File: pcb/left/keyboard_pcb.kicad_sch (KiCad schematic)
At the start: 42 parts, among them K00 KEYSW, K01 KEYSW, K02 KEYSW, K03 KEYSW, K04 KEYSW, K05 KEYSW, K10 KEYSW, K11 KEYSW, K12 KEYSW, K13 KEYSW, K14 KEYSW, K15 KEYSW, K20 KEYSW, K21 KEYSW, K22 KEYSW, K23 KEYSW, K24 KEYSW, K25 KEYSW, K30 KEYSW, K31 KEYSW, K32 KEYSW, U1 Flippable RP2040 ProMicro/nic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

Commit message: Update matrix schematic
 * Add diodes
 * Add 5-way nav. switches
 * Duplicate left to right
 * Tidy layout
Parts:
- added 右D00, 右D01, 右D02, 右D03, 右D04, 右D05, 右D10, 右D11, 右D12, 右D13, 右D14, 右D15, 右D20, 右D21, 右D22, 右D23, 右D24, 右D25, 右D32, 右D33, 右D34, 右D35, 右D40, 右D41, 右D42, 右D43, 右D44, 左D00, 左D01, 左D02, 左D03, 左D04, 左D05, 左D10, 左D11, 左D12, 左D13, 左D14, 左D15, 左D20, 左D21, 左D22, 左D23, 左D24, 左D25, 左D32, 左D33, 左D34, 左D35, 左D40, 左D41, 左D42, 左D43, 左D44: D, symbol Device:D
- added 右K00, 右K01, 右K02, 右K03, 右K04, 右K05, 右K10, 右K11, 右K12, 右K13, 右K14, 右K15, 右K20, 右K21, 右K22, 右K23, 右K24, 右K25, 右K33, 右K34, 右K35: KEYSW, keyswitches:SW_PG1350_reversible, symbol Switch:SW_Push
- added 右K43, 右K45, 左K43, 左K45: SW_SP5T, symbol _Project Library:SW_SP5T
- 左K00: renamed from K00; symbol keyboard_parts:KEYSW -> Switch:SW_Push
- 左K01: renamed from K01; symbol keyboard_parts:KEYSW -> Switch:SW_Push
- 左K02: renamed from K02; symbol keyboard_parts:KEYSW -> Switch:SW_Push
- 左K03: renamed from K03; symbol keyboard_parts:KEYSW -> Switch:SW_Push
- 左K04: renamed from K04; symbol keyboard_parts:KEYSW -> Switch:SW_Push
- 左K05: renamed from K05; symbol keyboard_parts:KEYSW -> Switch:SW_Push
- 左K10: renamed from K10; symbol keyboard_parts:KEYSW -> Switch:SW_Push
- 左K11: renamed from K11; symbol keyboard_parts:KEYSW -> Switch:SW_Push
- 左K12: renamed from K12; symbol keyboard_parts:KEYSW -> Switch:SW_Push
- 左K13: renamed from K13; symbol keyboard_parts:KEYSW -> Switch:SW_Push
- 左K14: renamed from K14; symbol keyboard_parts:KEYSW -> Switch:SW_Push
- 左K15: renamed from K15; symbol keyboard_parts:KEYSW -> Switch:SW_Push
- 左K20: renamed from K20; symbol keyboard_parts:KEYSW -> Switch:SW_Push
- 左K21: renamed from K21; symbol keyboard_parts:KEYSW -> Switch:SW_Push
- 左K22: renamed from K22; symbol keyboard_parts:KEYSW -> Switch:SW_Push
- 左K23: renamed from K23; symbol keyboard_parts:KEYSW -> Switch:SW_Push
- 左K24: renamed from K24; symbol keyboard_parts:KEYSW -> Switch:SW_Push
- 左K25: renamed from K25; symbol keyboard_parts:KEYSW -> Switch:SW_Push
- 左K33: renamed from K30; symbol keyboard_parts:KEYSW -> Switch:SW_Push
- 左K34: renamed from K31; symbol keyboard_parts:KEYSW -> Switch:SW_Push
- 左K35: renamed from K32; symbol keyboard_parts:KEYSW -> Switch:SW_Push
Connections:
- net col6 is gone; now on net col5: U1.24 (GP21/GP9)
- net k01 is gone; now on net col1: 左K01.1
- net k02 is gone; now on net col2: 左K02.1
- net k03 is gone; now on net col3: 左K03.1
- net k04 is gone; now on net col4: 左K04.1
- net k05 is gone; now on net col5: 左K05.1
- net k10 is gone; now on net col0: 左K10.1
- net k11 is gone; now on net col1: 左K11.1
- net k12 is gone; now on net col2: 左K12.1
- net k13 is gone; now on net col3: 左K13.1
- net k14 is gone; now on net col4: 左K14.1
- net k15 is gone; now on net col5: 左K15.1
- net k20 is gone; now on net col0: 左K20.1
- net k21 is gone; now on net col1: 左K21.1
- net k22 is gone; now on net col2: 左K22.1
- net k23 is gone; now on net col3: 左K23.1
- net k24 is gone; now on net col4: 左K24.1
- net k25 is gone; now on net col5: 左K25.1
- net k30 is gone; now on net col3: 左K33.1
- net k31 is gone; now on net col4: 左K34.1
- net k32 is gone; now on net col5: 左K35.1
- net row5 is gone; now on net row4: U1.12 (GP9/GP21)
- net GND: no longer 左K00.2, 左K01.2, 左K02.2, 左K03.2, 左K04.2, 左K05.2, 左K10.2, 左K11.2, 左K12.2, 左K13.2, 左K14.2, 左K15.2, 左K20.2, 左K21.2, 左K22.2, 左K23.2, 左K24.2, 左K25.2, 左K33.2, 左K34.2, 左K35.2
- net col1: now also U1.20 (GP26/GP5), 右D41.2 (A), 右K01.1, 右K11.1, 右K21.1, 左D41.2 (A); no longer U1.19 (GP27/GP4)
- net col2: now also U1.21 (GP22/GP6), 右E1.S1, 左E1.S1, 右D42.2 (A), 右K02.1, 右K12.1, 右K22.1, 左D42.2 (A); no longer U1.20 (GP26/GP5)
- net col3: now also U1.22 (GP20/GP7), 右D43.2 (A), 右K03.1, 右K13.1, 右K23.1, 右K33.1, 左D43.2 (A); no longer U1.21 (GP22/GP6)
- net col4: now also U1.23 (GP23/GP8), 右D44.2 (A), 右K04.1, 右K14.1, 右K24.1, 右K34.1, 左D44.2 (A); no longer U1.22 (GP20/GP7)
- net col5: now also 右K05.1, 右K15.1, 右K25.1, 右K35.1; no longer U1.23 (GP23/GP8)
- net row1: now also U1.9 (GP6/GP22), 右D10.1 (K), 右D11.1 (K), 右D12.1 (K), 右D13.1 (K), 右D14.1 (K), 右D15.1 (K), 左D10.1 (K), 左D11.1 (K), 左D12.1 (K), 左D13.1 (K), 左D14.1 (K), 左D15.1 (K); no longer U1.8 (GP5/GP26)
- net row2: now also U1.10 (GP7/GP20), 右D20.1 (K), 右D21.1 (K), 右D22.1 (K), 右D23.1 (K), 右D24.1 (K), 右D25.1 (K), 左D20.1 (K), 左D21.1 (K), 左D22.1 (K), 左D23.1 (K), 左D24.1 (K), 左D25.1 (K); no longer U1.9 (GP6/GP22)
- net row3: now also U1.11 (GP8/GP23), 右D32.1 (K), 右D33.1 (K), 右D34.1 (K), 右D35.1 (K), 左D32.1 (K), 左D33.1 (K), 左D34.1 (K), 左D35.1 (K); no longer U1.10 (GP7/GP20)
- net row4: now also 右K43.1, 右K45.1, 左K43.1, 左K45.1; no longer U1.11 (GP8/GP23)
- net at 右E1.S2: now also 右D32.2 (A)
- net at 左E1.S2: now also 左D32.2 (A)
- net k00 renamed col0
- net col0: now also U1.19 (GP27/GP4), 右D40.2 (A), 右K00.1, 右K10.1, 右K20.1, 左D40.2 (A)
- new net: 右D21.2 (A), 右K21.2
- new net: 左D35.2 (A), 左K35.2
- new net: 左D13.2 (A), 左K13.2
- new net: 右D22.2 (A), 右K22.2
- new net: 左D24.2 (A), 左K24.2
- new net: 右D00.2 (A), 右K00.2
- new net: 右D23.2 (A), 右K23.2
- new net: 左D05.2 (A), 左K05.2
- new net: 右D25.2 (A), 右K25.2
- new net: 右D01.2 (A), 右K01.2
- new net: 右D02.2 (A), 右K02.2
- new net: 左D20.2 (A), 左K20.2
- new net: 左D11.2 (A), 左K11.2
- new net: 右D34.2 (A), 右K34.2
- new net: 右D24.2 (A), 右K24.2
- new net: 右D35.2 (A), 右K35.2
- new net: 左D00.2 (A), 左K00.2
- new net: 右D20.2 (A), 右K20.2
- new net: 右D14.2 (A), 右K14.2
- new net: 左D14.2 (A), 左K14.2
- new net: 左D15.2 (A), 左K15.2
- new net: 左D42.1 (K), 左K43.4, 左K45.4
- new net: 右D03.2 (A), 右K03.2
- new net: 右D33.2 (A), 右K33.2
- new net: 右D04.2 (A), 右K04.2
- new net: 右D41.1 (K), 右K43.3, 右K45.3
- new net: 右D05.2 (A), 右K05.2
- new net: 左D03.2 (A), 左K03.2
- new net: 右D44.1 (K), 右K43.6, 右K45.6
- new net: 左D43.1 (K), 左K43.5, 左K45.5
- new net: 左D22.2 (A), 左K22.2
- new net: 左D40.1 (K), 左K43.2, 左K45.2
- new net: 左D41.1 (K), 左K43.3, 左K45.3
- new net: 左D44.1 (K), 左K43.6, 左K45.6
- new net: 左D02.2 (A), 左K02.2
- new net: 右D13.2 (A), 右K13.2
- new net: 左D33.2 (A), 左K33.2
- new net: 右D43.1 (K), 右K43.5, 右K45.5
- new net: 右D42.1 (K), 右K43.4, 右K45.4
- new net: 右D11.2 (A), 右K11.2
- new net: 左D04.2 (A), 左K04.2
- new net: 左D12.2 (A), 左K12.2
- new net: 左D23.2 (A), 左K23.2
- new net: 右D10.2 (A), 右K10.2
- new net: 左D25.2 (A), 左K25.2
- new net: 右D12.2 (A), 右K12.2
- new net: 左D10.2 (A), 左K10.2
- new net: 左D01.2 (A), 左K01.2
- new net: 左D34.2 (A), 左K34.2
- new net: 右D40.1 (K), 右K43.2, 右K45.2
- new net: 左D21.2 (A), 左K21.2
- new net: 右D15.2 (A), 右K15.2
- new net row0: U1.8 (GP5/GP26), 右D00.1 (K), 右D01.1 (K), 右D02.1 (K), 右D03.1 (K), 右D04.1 (K), 右D05.1 (K), 左D00.1 (K), 左D01.1 (K), 左D02.1 (K), 左D03.1 (K), 左D04.1 (K), 左D05.1 (K)
- no-connect marks 0 -> 2
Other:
- moved on the sheet: H1, H2, H3, H4, MB1, MB2, MB3, MB4, U1, 右J1, 右J2, 右L2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

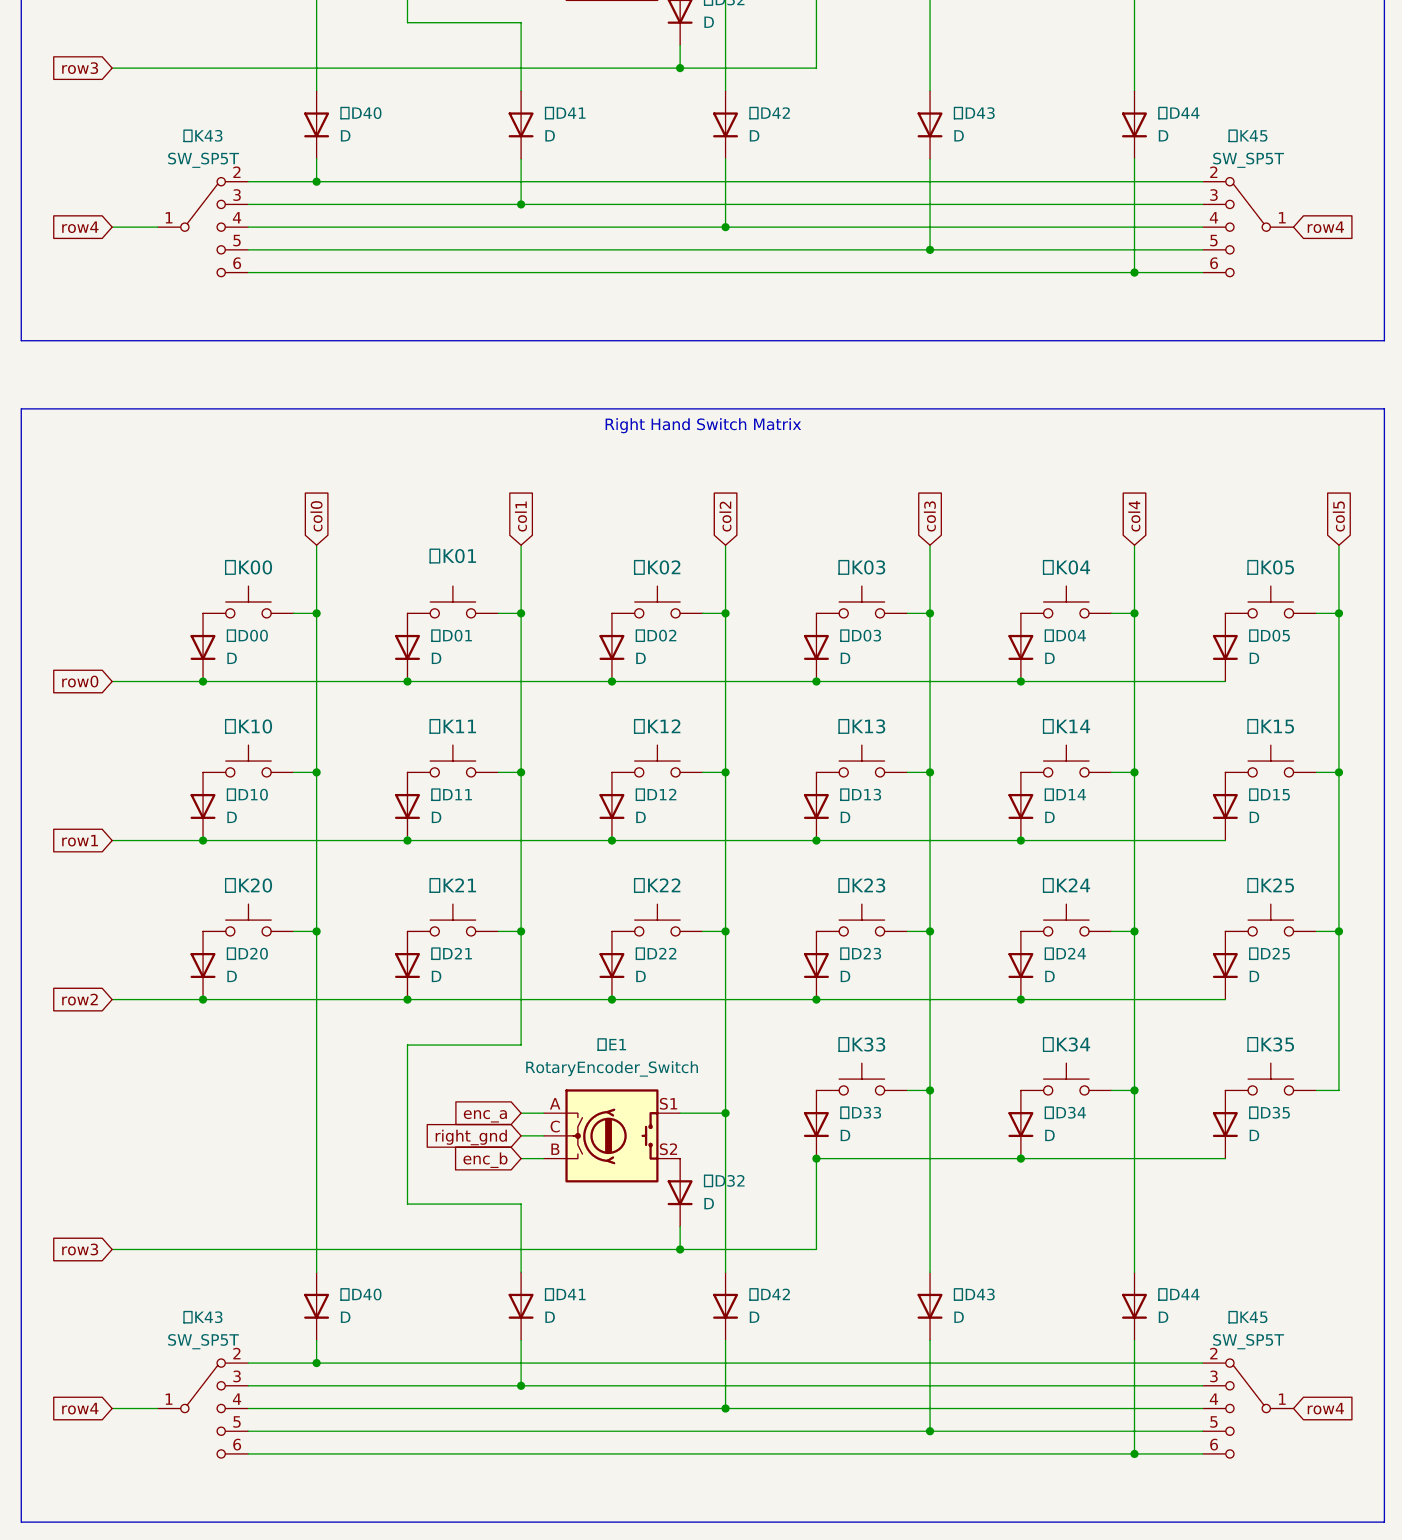
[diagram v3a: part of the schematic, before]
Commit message: Update nav. switch symbol to match datasheet
https://www.mouser.com/datasheet/2/15/SKRH-1370966.pdf
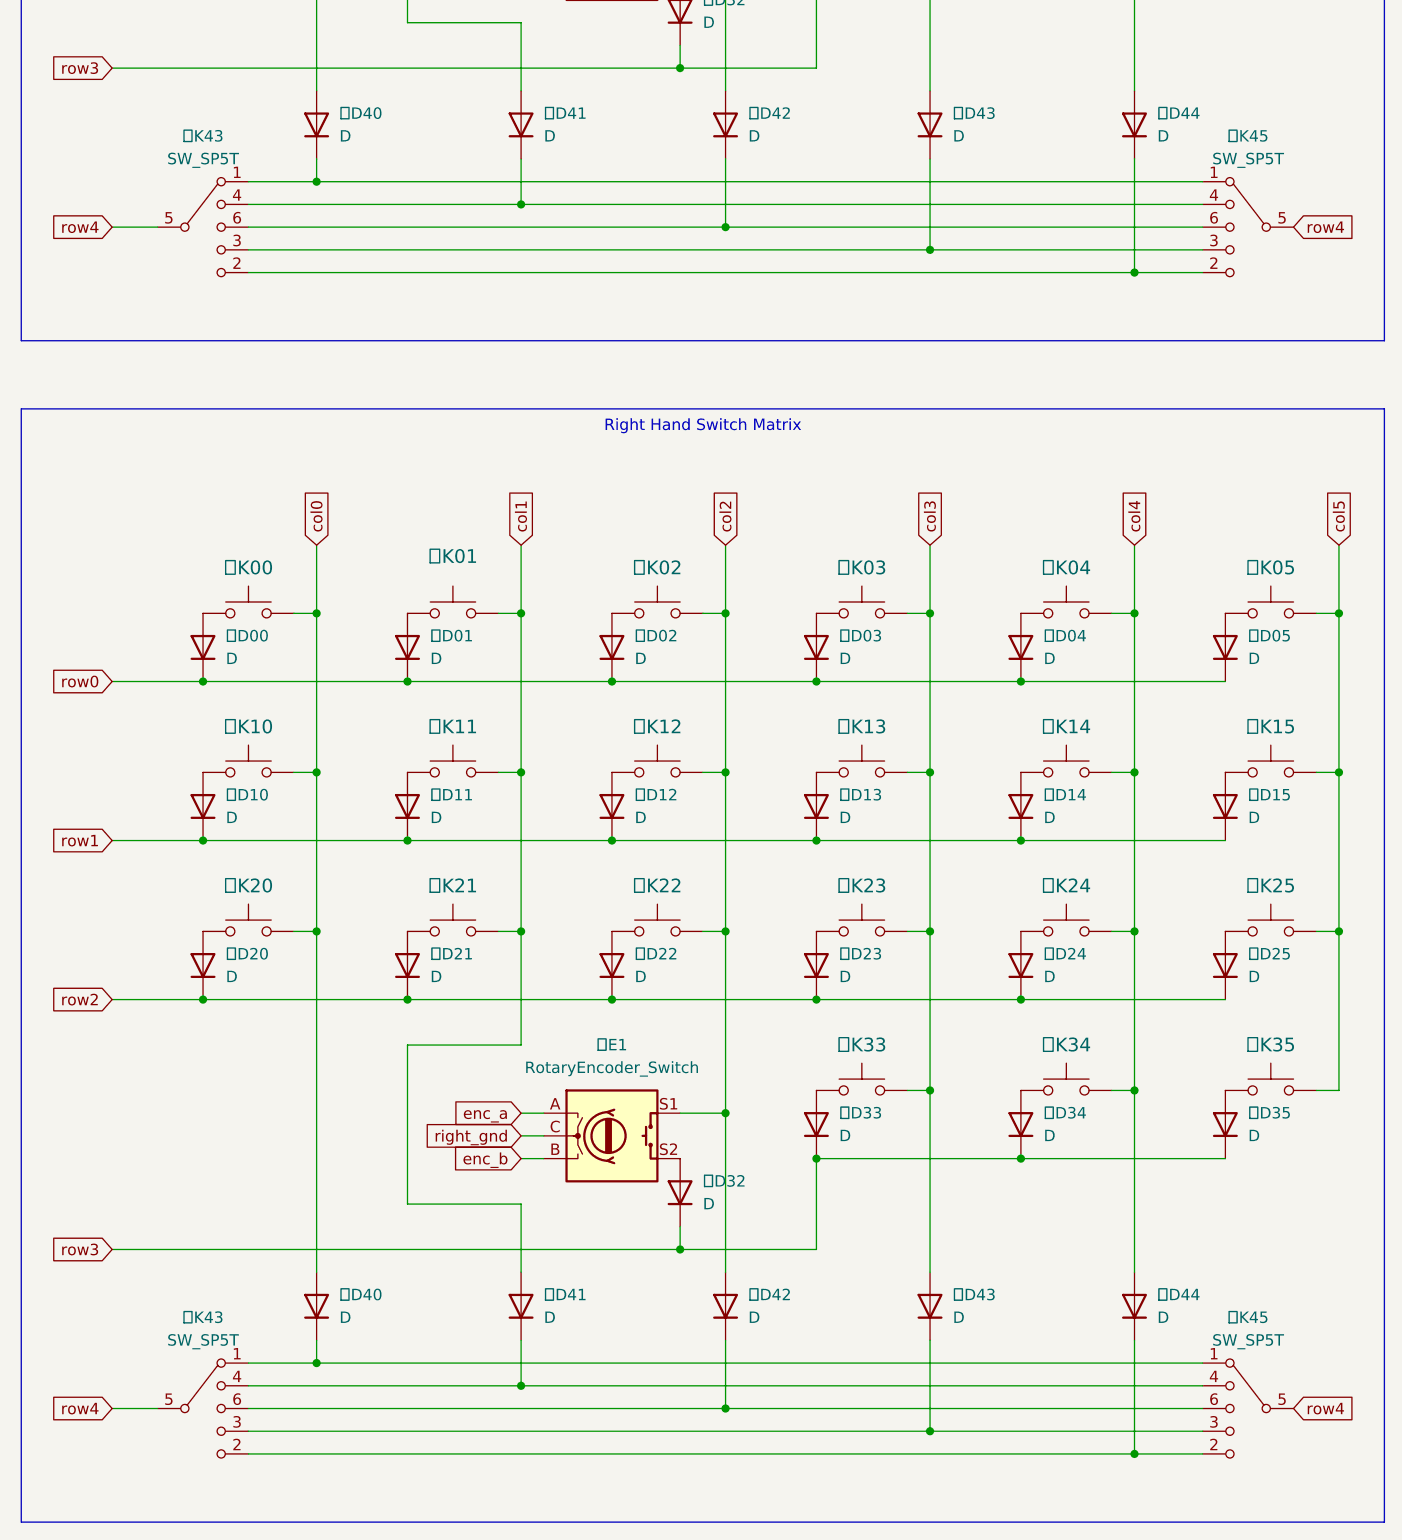
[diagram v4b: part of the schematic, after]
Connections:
- net row4: now also 右K43.5 (Com), 右K45.5 (Com), 左K43.5 (Com), 左K45.5 (Com); no longer 右K43.1, 右K45.1, 左K43.1, 左K45.1
- net at 左K43.4 (B), 左K45.4 (B): now also 左D41.1 (K); no longer 左D42.1 (K)
- net at 右K43.3 (C), 右K45.3 (C): now also 右D43.1 (K); no longer 右D41.1 (K)
- net at 右K43.6 (D), 右K45.6 (D): now also 右D42.1 (K); no longer 右D44.1 (K)
- net at 左K43.2 (Ctr), 左K45.2 (Ctr): now also 左D44.1 (K); no longer 左D40.1 (K)
- net at 左K43.3 (C), 左K45.3 (C): now also 左D43.1 (K); no longer 左D41.1 (K)
- net at 左K43.6 (D), 左K45.6 (D): now also 左D42.1 (K); no longer 左D44.1 (K)
- net at 右K43.4 (B), 右K45.4 (B): now also 右D41.1 (K); no longer 右D42.1 (K)
- net at 右K43.2 (Ctr), 右K45.2 (Ctr): now also 右D44.1 (K); no longer 右D40.1 (K)
- new net: 左D40.1 (K), 左K43.1 (A), 左K45.1 (A)
- new net: 右D40.1 (K), 右K43.1 (A), 右K45.1 (A)

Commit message: Assign footprints
TODO:

 * Reassign mounting holes — these seem to have been renamed, so the schematic no longer matches the linked library
 * Create mirrorable MCU footprint
 * Decide on reset switch
 * Create mirrorable hot-swap switch footprint(s)
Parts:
- U1: footprint PCM_marbastlib-xp-promicroish:ProMicro_USBup -> (none)
- 右D00, 右D01, 右D02, 右D03, 右D04, 右D05, 右D10, 右D11, 右D12, 右D13, 右D14, 右D15, 右D20, 右D21, 右D22, 右D23, 右D24, 右D25, 右D32, 右D33, 右D34, 右D35, 右D40, 右D41, 右D42, 右D43, 右D44, 左D00, 左D01, 左D02, 左D03, 左D04, 左D05, 左D10, 左D11, 左D12, 左D13, 左D14, 左D15, 左D20, 左D21, 左D22, 左D23, 左D24, 左D25, 左D32, 左D33, 左D34, 左D35, 左D40, 左D41, 左D42, 左D43, 左D44: footprint (none) -> Diode_SMD:D_SOD-123
- 右E1, 左E1: footprint (none) -> _Project Library:RollerEncoder_Panasonic_EVQWGD001
- 右J1, 左J1: footprint (none) -> Connector_JST:JST_GH_SM02B-GHS-TB_1x02-1MP_P1.25mm_Horizontal
- 右J2, 右S2, 左J2: footprint (none) -> _Project Library:USB_C_Receptacle_GCT_USB4125-xx-x_6P_TopMnt_Horizontal_Flippable
- 右K00, 右K01, 右K02, 右K03, 右K04, 右K05, 右K10, 右K11, 右K12, 右K13, 右K14, 右K15, 右K20, 右K21, 右K22, 右K23, 右K24, 右K25, 右K33, 右K34, 右K35: footprint keyswitches:SW_PG1350_reversible -> Diode_SMD:D_SOD-123
- 右K43, 右K45, 左K43, 左K45: footprint (none) -> _Project Library:Nav_Switch_SKRHAxE010
- 右L2, 左L1: footprint LED_SMD:LED_SK6812MINI_PLCC4_3.5x3.5mm_P1.75mm -> beekeeb_lib:SK6812-MINI-E
- 右S1, 左S1: footprint (none) -> _Project Library:SW_MSK12C02-HB_Flippable
